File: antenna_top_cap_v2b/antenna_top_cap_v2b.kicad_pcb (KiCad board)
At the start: 4 copper layers, 100 x 100 mm, 48 parts, among them J1 DEBUG, J12 USB_C_Receptacle_USB2.0_16P, J2 Battery Charge Bypass, J3 FC Reset Jumper, J4 FC USB Bootselect Jumper, J5 Conn_Coaxial, Q1 BSS138, U1 VL6180XV0NR/1, U16 MCP9808T-E/MS, U2 LP5907-2.8V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

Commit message: Added Payload USB Passthrough
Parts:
- added J8: USB_C_Receptacle_USB2.0_16P, Connector_USB:USB_C_Receptacle_HRO_TYPE-C-31-M-12, B.Cu at (186.4, 66.7)
- added J9: Conn_02x02_Odd_Even, Connector_Hirose:Hirose_DF11-4DP-2DSA_2x02_P2.00mm_Vertical, F.Cu at (185.9, 75.1)
- added R5: 5.1k, Resistor_SMD:R_0603_1608Metric, F.Cu at (183.4, 72.3)
- added R6: 5.1k, Resistor_SMD:R_0603_1608Metric, F.Cu at (189.7, 72.3)
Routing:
- net /Payload_VBUS: track 0.00 -> 14.9 mm
- net GND: track 82.1 -> 92.3 mm, vias 27 -> 29
- net /Payload_D-: track 0.00 -> 9.49 mm
- net /Payload_D+: track 0.00 -> 8.75 mm, vias 0 -> 2
- net Net-(J8-CC2): track 0.00 -> 2.35 mm, vias 0 -> 1
- net Net-(J8-CC1): track 0.00 -> 2.20 mm, vias 0 -> 1

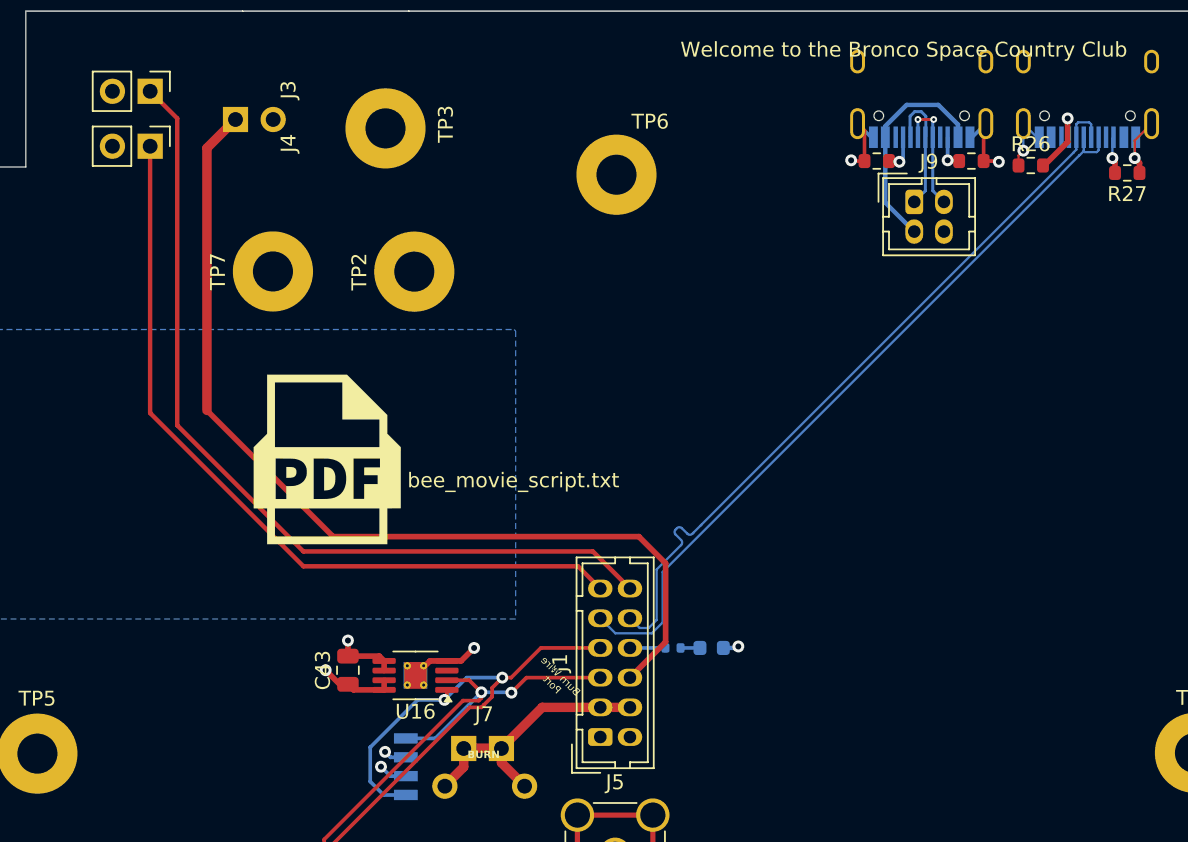
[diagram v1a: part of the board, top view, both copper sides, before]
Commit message: Redid USB Trace Impedance
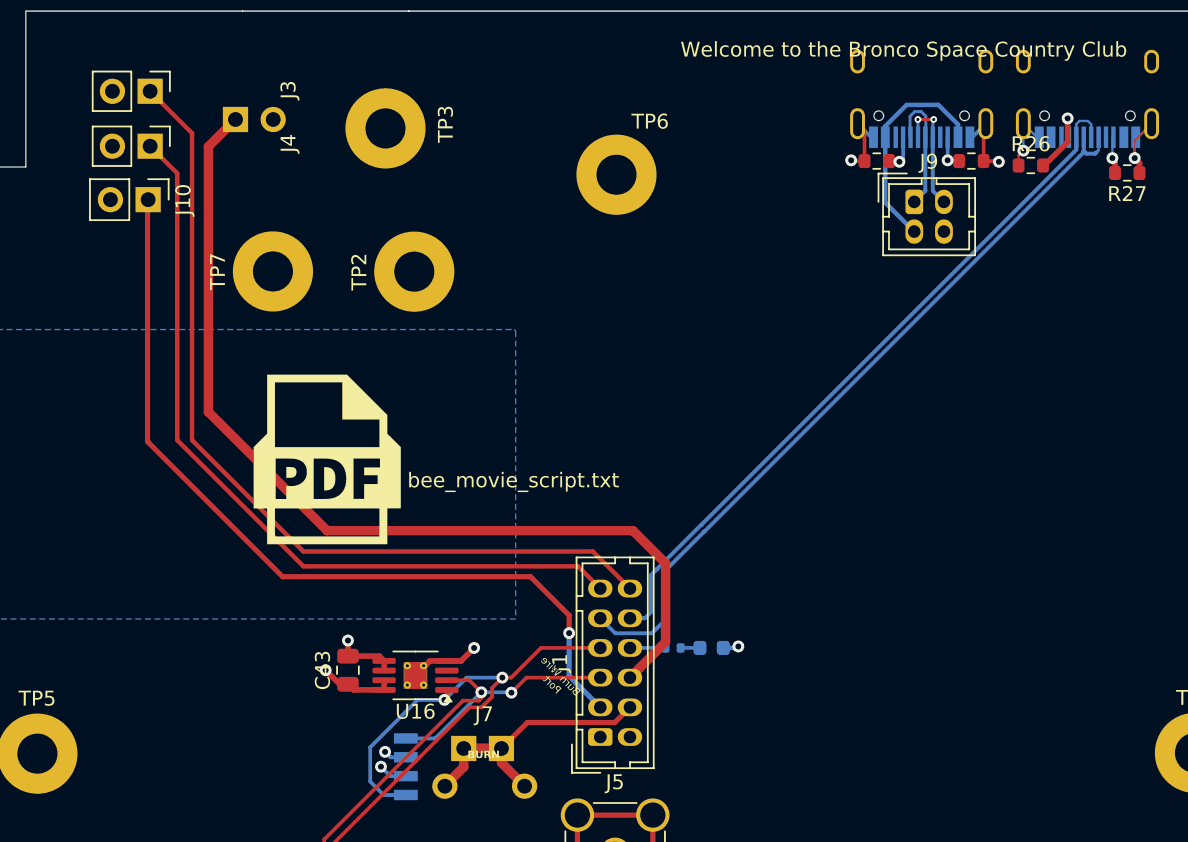
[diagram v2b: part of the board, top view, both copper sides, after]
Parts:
- added J10: WDT Disable Jumper, Connector_PinHeader_2.54mm:PinHeader_1x02_P2.54mm_Vertical, F.Cu at (134.3, 74.9)
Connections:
- J1 pad 3: BURN -> WDT_DISABLE
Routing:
- net WDT_DISABLE: track 0.00 -> 56.6 mm, vias 0 -> 1
- net USB_D-: track 50.9 -> 48.4 mm
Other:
- board text added: "WDT DISABLE"

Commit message: Added Alt RBF
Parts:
- added C4: 100nF, Capacitor_SMD:C_0805_2012Metric, F.Cu at (126.7, 135.8)
- added C5: 100nF, Capacitor_SMD:C_0805_2012Metric, F.Cu at (147.9, 112.2)
- added J11: DF11-4DP-2DSA, Connector_Hirose:Hirose_DF11-4DP-2DSA_2x02_P2.00mm_Vertical, F.Cu at (202.5, 77.6)
- added J13: DNP, Connector_Hirose:Hirose_DF11-4DP-2DSA_2x02_P2.00mm_Vertical, F.Cu at (198.0, 77.8)
- added Q2: CSD17576Q5B, Package_TO_SOT_SMD:TDSON-8-1, F.Cu at (200.6, 88.0)
- added R7: 1M, Resistor_SMD:R_0603_1608Metric, F.Cu at (199.5, 83.1)
- C43: value 1uF -> 100nF
- J9: value Conn_02x02_Odd_Even -> DF11-4DP-2DSA
- moved G*** 7.26 mm to (193.8, 95.0)
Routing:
- net Net-(J13-Pin_1): track 0.00 -> 7.59 mm
- net /RBF_High: track 0.00 -> 6.40 mm
- net GND: track 92.3 -> 94.4 mm, vias 29 -> 31
- net 2.8V: track 49.8 -> 51.3 mm
- net +3V3: track 24.6 -> 26.0 mm
- added copper zone on F.Cu, net /RBF_High
- added copper zone on F.Cu, net /RBF_Low
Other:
- board text added: "ALT RBF Jump Right to Left to Disable Battery"
